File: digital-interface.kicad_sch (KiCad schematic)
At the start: 37 parts, among them U701 Si8641BD-B-IS2, U702 R05C05TE05S

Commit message: add enclosure dac sub circuit
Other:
- title: Enclosure -> Power Supply Sink
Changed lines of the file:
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@@
 	(paper "A4")
 	(title_block
-		(title "Enclosure")
+		(title "Power Supply Sink")
 		(date "2025-02-20")
-		(rev "0.1.0")
+		(rev "0.2.0")
 		(company "Open Battery Tester")
 		(comment 1 "Digital Interface")

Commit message: add enclosure power sub circuit
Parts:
- D701, D702, D704, D705: MPN UDD32C15L01 -> UDD32C24L01; VPN 603-UDD32C15L01 -> 603-UDD32C24L01
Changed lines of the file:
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@@
 		(title "Power Supply Sink")
 		(date "2025-02-20")
-		(rev "0.4.0")
+		(rev "0.5.0")
 		(company "Open Battery Tester")
 		(comment 1 "Digital Interface")
@@
 			)
 		)
-		(property "MPN" "UDD32C15L01"
+		(property "MPN" "UDD32C24L01"
 			(at 49.53 85.09 0)
 			(effects
@@
 			)
 		)
-		(property "VPN" "603-UDD32C15L01"
+		(property "VPN" "603-UDD32C24L01"
 			(at 49.53 85.09 0)
 			(effects
@@
 			)
 		)
-		(property "MPN" "UDD32C15L01"
+		(property "MPN" "UDD32C24L01"
 			(at 62.23 85.09 0)
 			(effects
@@
 			)
 		)
-		(property "VPN" "603-UDD32C15L01"
+		(property "VPN" "603-UDD32C24L01"
 			(at 62.23 85.09 0)
 			(effects
@@
 			)
 		)
-		(property "MPN" "UDD32C15L01"
+		(property "MPN" "UDD32C24L01"
 			(at 74.93 85.09 0)
 			(effects
@@
 			)
 		)
-		(property "VPN" "603-UDD32C15L01"
+		(property "VPN" "603-UDD32C24L01"
 			(at 74.93 85.09 0)
 			(effects
@@
 			)
 		)
-		(property "MPN" "UDD32C15L01"
+		(property "MPN" "UDD32C24L01"
 			(at 87.63 85.09 0)
 			(effects
@@
 			)
 		)
-		(property "VPN" "603-UDD32C15L01"
+		(property "VPN" "603-UDD32C24L01"
 			(at 87.63 85.09 0)
 			(effects

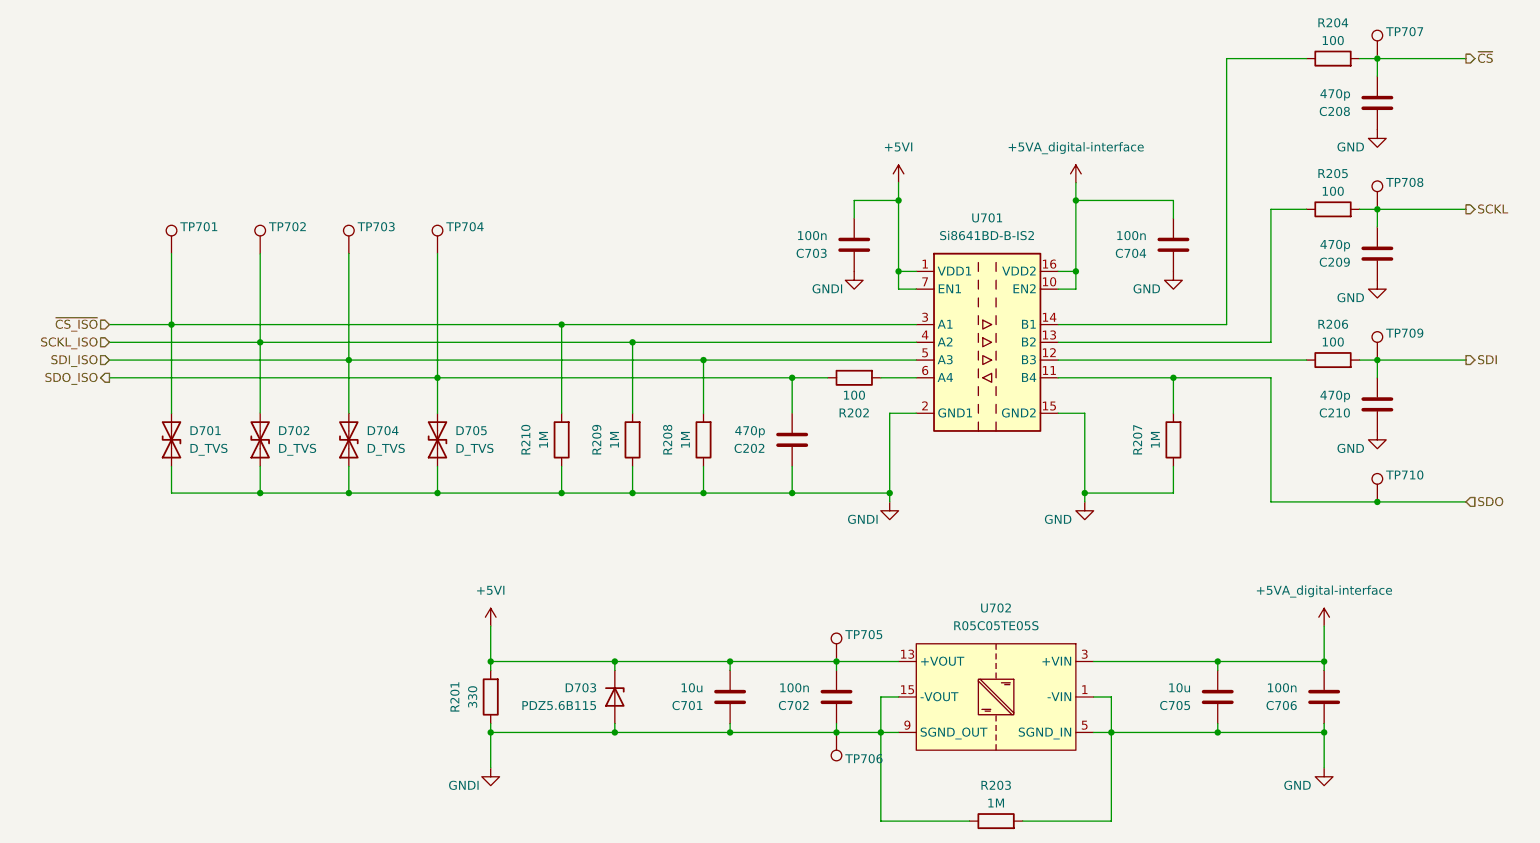
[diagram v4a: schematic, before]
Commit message: add enclosure output connectors
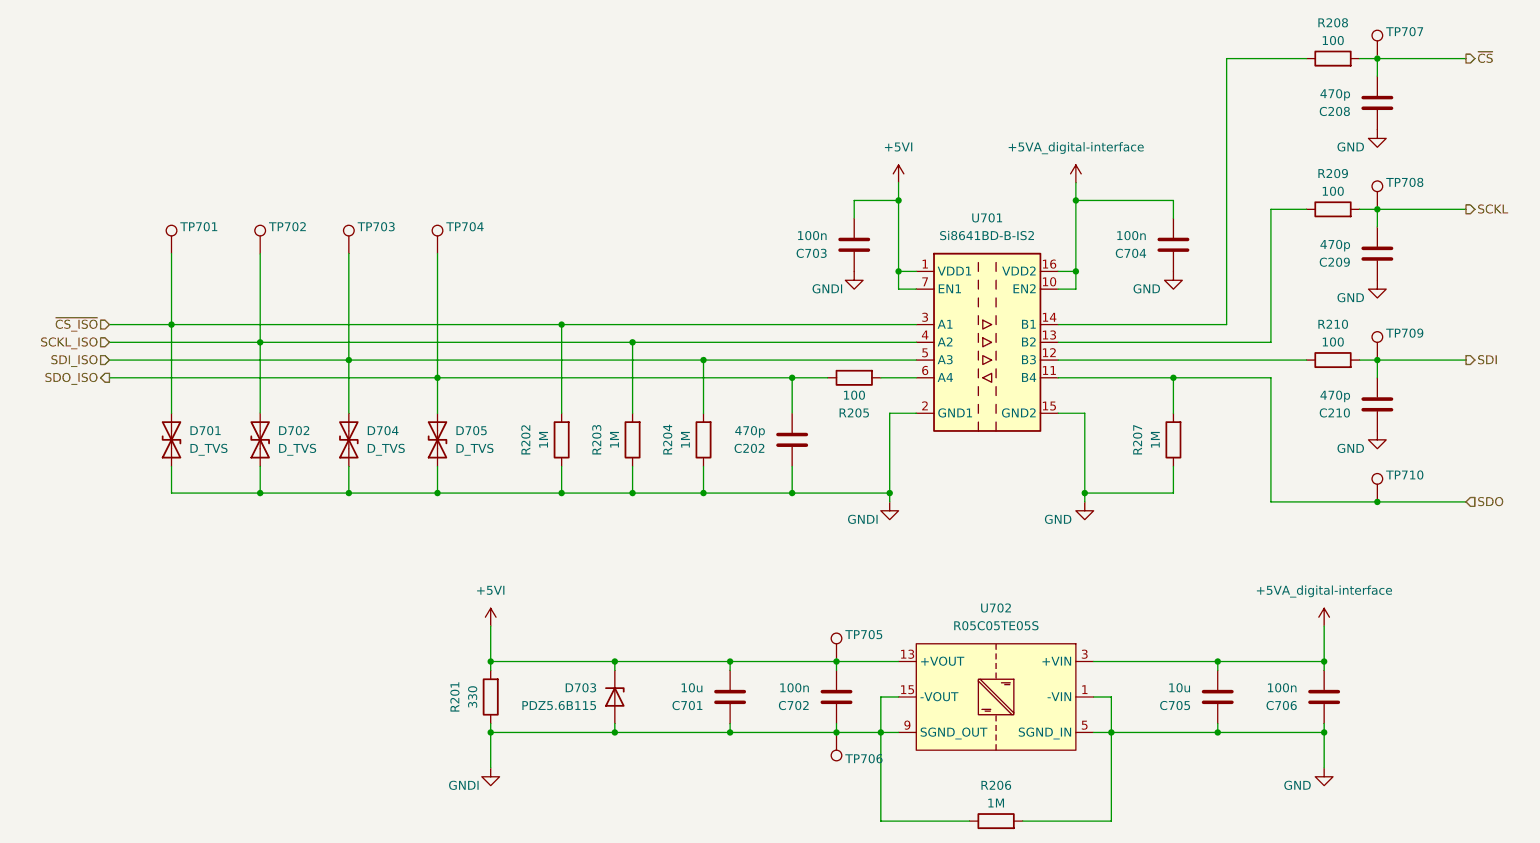
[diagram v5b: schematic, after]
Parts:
- renumbered R210 to R202, R209 to R203, R208 to R204, R202 to R205, R203 to R206, R204 to R208, R205 to R209, R206 to R210
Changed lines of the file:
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@@
 	(title_block
 		(title "Power Supply Sink")
-		(date "2025-02-20")
-		(rev "0.5.0")
+		(date "2025-02-21")
+		(rev "1.0.0")
 		(company "Open Battery Tester")
 		(comment 1 "Digital Interface")
@@
 		(on_board yes)
 		(dnp no)
-		(property "Reference" "R202"
+		(property "Reference" "R205"
 			(at 147.32 81.28 90)
 			(effects
@@
 			(project "enclosure"
 				(path "/8ec0899b-9d7b-491d-933a-49b74b34a0df/dc44c087-3b63-4db9-8fc8-89acb3b8154a"
-					(reference "R202")
+					(reference "R205")
 					(unit 1)
 				)
@@
 		(on_board yes)
 		(dnp no)
-		(property "Reference" "R203"
+		(property "Reference" "R206"
 			(at 167.64 134.62 90)
 			(effects
@@
 			(project "enclosure"
 				(path "/8ec0899b-9d7b-491d-933a-49b74b34a0df/dc44c087-3b63-4db9-8fc8-89acb3b8154a"
-					(reference "R203")
+					(reference "R206")
 					(unit 1)
 				)
@@
 		(on_board yes)
 		(dnp no)
-		(property "Reference" "R208"
+		(property "Reference" "R204"
 			(at 120.65 85.09 90)
 			(effects
@@
 			(project "enclosure"
 				(path "/8ec0899b-9d7b-491d-933a-49b74b34a0df/dc44c087-3b63-4db9-8fc8-89acb3b8154a"
-					(reference "R208")
+					(reference "R204")
 					(unit 1)
 				)
@@
 		(on_board yes)
 		(dnp no)
-		(property "Reference" "R204"
+		(property "Reference" "R208"
 			(at 215.9 25.4 90)
 			(effects
@@
 			(project "enclosure"
 				(path "/8ec0899b-9d7b-491d-933a-49b74b34a0df/dc44c087-3b63-4db9-8fc8-89acb3b8154a"
-					(reference "R204")
+					(reference "R208")
 					(unit 1)
 				)
@@
 		(on_board yes)
 		(dnp no)
-		(property "Reference" "R205"
+		(property "Reference" "R209"
 			(at 215.9 46.99 90)
 			(effects
@@
 			(project "enclosure"
 				(path "/8ec0899b-9d7b-491d-933a-49b74b34a0df/dc44c087-3b63-4db9-8fc8-89acb3b8154a"
-					(reference "R205")
+					(reference "R209")
 					(unit 1)
 				)
@@
 		(on_board yes)
 		(dnp no)
-		(property "Reference" "R206"
+		(property "Reference" "R210"
 			(at 215.9 68.58 90)
 			(effects
@@
 			(project "enclosure"
 				(path "/8ec0899b-9d7b-491d-933a-49b74b34a0df/dc44c087-3b63-4db9-8fc8-89acb3b8154a"
-					(reference "R206")
+					(reference "R210")
 					(unit 1)
 				)
@@
 		(on_board yes)
 		(dnp no)
-		(property "Reference" "R210"
+		(property "Reference" "R202"
 			(at 100.33 85.09 90)
 			(effects
@@
 			(project "enclosure"
 				(path "/8ec0899b-9d7b-491d-933a-49b74b34a0df/dc44c087-3b63-4db9-8fc8-89acb3b8154a"
-					(reference "R210")
+					(reference "R202")
 					(unit 1)
 				)
@@
 		(on_board yes)
 		(dnp no)
-		(property "Reference" "R209"
+		(property "Reference" "R203"
 			(at 110.49 85.09 90)
 			(effects
@@
 			(project "enclosure"
 				(path "/8ec0899b-9d7b-491d-933a-49b74b34a0df/dc44c087-3b63-4db9-8fc8-89acb3b8154a"
-					(reference "R209")
+					(reference "R203")
 					(unit 1)
 				)

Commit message: update datasheets and footprint references
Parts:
- C202, C208, C209, C210, C702, C703, C704, C706: footprint pss:C_0805_2012Metric_Pad1.18x1.45mm_HandSolder -> enclosure:C_0805_2012Metric_Pad1.18x1.45mm_HandSolder
- C701, C705: footprint pss:C_1210_3225Metric_Pad1.33x2.70mm_HandSolder -> enclosure:C_1210_3225Metric_Pad1.33x2.70mm_HandSolder
- D701, D702, D703, D704, D705: footprint pss:D_SOD-323_HandSoldering -> enclosure:D_SOD-323_HandSoldering
- R201, R202, R203, R204, R205, R206, R207, R208, R209, R210: footprint pss:R_1210_3225Metric_Pad1.30x2.65mm_HandSolder -> enclosure:R_1210_3225Metric_Pad1.30x2.65mm_HandSolder
- TP701, TP702, TP703, TP704, TP705, TP706, TP707, TP708, TP709, TP710: footprint pss:TP_0805_2012Metric -> enclosure:TP_0805_2012Metric
- U701, U702: footprint pss:SOIC-16W_7.5x10.3mm_P1.27mm -> enclosure:SOIC-16W_7.5x10.3mm_P1.27mm
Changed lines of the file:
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@@
 			)
 		)
-		(property "Footprint" "pss:D_SOD-323_HandSoldering"
+		(property "Footprint" "enclosure:D_SOD-323_HandSoldering"
 			(at 49.53 85.09 0)
 			(effects
@@
 			)
 		)
-		(property "Footprint" "pss:D_SOD-323_HandSoldering"
+		(property "Footprint" "enclosure:D_SOD-323_HandSoldering"
 			(at 62.23 85.09 0)
 			(effects
@@
 			)
 		)
-		(property "Footprint" "pss:C_0805_2012Metric_Pad1.18x1.45mm_HandSolder"
+		(property "Footprint" "enclosure:C_0805_2012Metric_Pad1.18x1.45mm_HandSolder"
 			(at 221.2848 33.02 0)
 			(effects
@@
 			)
 		)
-		(property "Footprint" "pss:C_0805_2012Metric_Pad1.18x1.45mm_HandSolder"
+		(property "Footprint" "enclosure:C_0805_2012Metric_Pad1.18x1.45mm_HandSolder"
 			(at 213.6648 118.11 0)
 			(effects
@@
 			)
 		)
-		(property "Footprint" "pss:TP_0805_2012Metric"
+		(property "Footprint" "enclosure:TP_0805_2012Metric"
 			(at 80.01 58.42 0)
 			(effects
@@
 			)
 		)
-		(property "Footprint" "pss:TP_0805_2012Metric"
+		(property "Footprint" "enclosure:TP_0805_2012Metric"
 			(at 227.33 52.07 0)
 			(effects
@@
 			)
 		)
-		(property "Footprint" "pss:C_0805_2012Metric_Pad1.18x1.45mm_HandSolder"
+		(property "Footprint" "enclosure:C_0805_2012Metric_Pad1.18x1.45mm_HandSolder"
 			(at 192.0748 53.34 0)
 			(effects
@@
 			)
 		)
-		(property "Footprint" "pss:TP_0805_2012Metric"
+		(property "Footprint" "enclosure:TP_0805_2012Metric"
 			(at 54.61 58.42 0)
 			(effects
@@
 			)
 		)
-		(property "Footprint" "pss:R_1210_3225Metric_Pad1.30x2.65mm_HandSolder"
+		(property "Footprint" "enclosure:R_1210_3225Metric_Pad1.30x2.65mm_HandSolder"
 			(at 147.32 74.422 90)
 			(effects
@@
 			)
 		)
-		(property "Footprint" "pss:C_1210_3225Metric_Pad1.33x2.70mm_HandSolder"
+		(property "Footprint" "enclosure:C_1210_3225Metric_Pad1.33x2.70mm_HandSolder"
 			(at 198.4248 118.11 0)
 			(effects
@@
 			)
 		)
-		(property "Footprint" "pss:R_1210_3225Metric_Pad1.30x2.65mm_HandSolder"
+		(property "Footprint" "enclosure:R_1210_3225Metric_Pad1.30x2.65mm_HandSolder"
 			(at 167.64 141.478 90)
 			(effects
@@
 			)
 		)
-		(property "Footprint" "pss:TP_0805_2012Metric"
+		(property "Footprint" "enclosure:TP_0805_2012Metric"
 			(at 227.33 93.98 0)
 			(effects
@@
 			)
 		)
-		(property "Footprint" "pss:R_1210_3225Metric_Pad1.30x2.65mm_HandSolder"
+		(property "Footprint" "enclosure:R_1210_3225Metric_Pad1.30x2.65mm_HandSolder"
 			(at 127.508 85.09 90)
 			(effects
@@
 			)
 		)
-		(property "Footprint" "pss:R_1210_3225Metric_Pad1.30x2.65mm_HandSolder"
+		(property "Footprint" "enclosure:R_1210_3225Metric_Pad1.30x2.65mm_HandSolder"
 			(at 215.9 32.258 90)
 			(effects
@@
 			)
 		)
-		(property "Footprint" "pss:D_SOD-323_HandSoldering"
+		(property "Footprint" "enclosure:D_SOD-323_HandSoldering"
 			(at 113.03 121.92 0)
 			(effects
@@
 			)
 		)
-		(property "Footprint" "pss:C_0805_2012Metric_Pad1.18x1.45mm_HandSolder"
+		(property "Footprint" "enclosure:C_0805_2012Metric_Pad1.18x1.45mm_HandSolder"
 			(at 221.2848 76.2 0)
 			(effects
@@
 			)
 		)
-		(property "Footprint" "pss:R_1210_3225Metric_Pad1.30x2.65mm_HandSolder"
+		(property "Footprint" "enclosure:R_1210_3225Metric_Pad1.30x2.65mm_HandSolder"
 			(at 97.028 121.92 90)
 			(effects
@@
 			)
 		)
-		(property "Footprint" "pss:TP_0805_2012Metric"
+		(property "Footprint" "enclosure:TP_0805_2012Metric"
 			(at 92.71 58.42 0)
 			(effects
@@
 			)
 		)
-		(property "Footprint" "pss:C_0805_2012Metric_Pad1.18x1.45mm_HandSolder"
+		(property "Footprint" "enclosure:C_0805_2012Metric_Pad1.18x1.45mm_HandSolder"
 			(at 221.2848 54.61 0)
 			(effects
@@
 			)
 		)
-		(property "Footprint" "pss:C_1210_3225Metric_Pad1.33x2.70mm_HandSolder"
+		(property "Footprint" "enclosure:C_1210_3225Metric_Pad1.33x2.70mm_HandSolder"
 			(at 128.5748 118.11 0)
 			(effects
@@
 			)
 		)
-		(property "Footprint" "pss:D_SOD-323_HandSoldering"
+		(property "Footprint" "enclosure:D_SOD-323_HandSoldering"
 			(at 74.93 85.09 0)
 			(effects
@@
 			)
 		)
-		(property "Footprint" "pss:R_1210_3225Metric_Pad1.30x2.65mm_HandSolder"
+		(property "Footprint" "enclosure:R_1210_3225Metric_Pad1.30x2.65mm_HandSolder"
 			(at 215.9 53.848 90)
 			(effects
@@
 			)
 		)
-		(property "Footprint" "pss:TP_0805_2012Metric"
+		(property "Footprint" "enclosure:TP_0805_2012Metric"
 			(at 227.33 73.66 0)
 			(effects
@@
 			)
 		)
-		(property "Footprint" "pss:SOIC-16W_7.5x10.3mm_P1.27mm"
+		(property "Footprint" "enclosure:SOIC-16W_7.5x10.3mm_P1.27mm"
 			(at 167.64 121.92 0)
 			(effects
@@
 			)
 		)
-		(property "Footprint" "pss:R_1210_3225Metric_Pad1.30x2.65mm_HandSolder"
+		(property "Footprint" "enclosure:R_1210_3225Metric_Pad1.30x2.65mm_HandSolder"
 			(at 215.9 75.438 90)
 			(effects
@@
 			)
 		)
-		(property "Footprint" "pss:TP_0805_2012Metric"
+		(property "Footprint" "enclosure:TP_0805_2012Metric"
 			(at 149.86 116.84 0)
 			(effects
@@
 			)
 		)
-		(property "Footprint" "pss:TP_0805_2012Metric"
+		(property "Footprint" "enclosure:TP_0805_2012Metric"
 			(at 67.31 58.42 0)
 			(effects
@@
 			)
 		)
-		(property "Footprint" "pss:C_0805_2012Metric_Pad1.18x1.45mm_HandSolder"
+		(property "Footprint" "enclosure:C_0805_2012Metric_Pad1.18x1.45mm_HandSolder"
 			(at 143.8148 118.11 0)
 			(effects
@@
 			)
 		)
-		(property "Footprint" "pss:TP_0805_2012Metric"
+		(property "Footprint" "enclosure:TP_0805_2012Metric"
 			(at 227.33 30.48 0)
 			(effects
@@
 			)
 		)
-		(property "Footprint" "pss:TP_0805_2012Metric"
+		(property "Footprint" "enclosure:TP_0805_2012Metric"
 			(at 149.86 127 0)
 			(effects
@@
 			)
 		)
-		(property "Footprint" "pss:R_1210_3225Metric_Pad1.30x2.65mm_HandSolder"
+		(property "Footprint" "enclosure:R_1210_3225Metric_Pad1.30x2.65mm_HandSolder"
 			(at 107.188 85.09 90)
 			(effects
@@
 			)
 		)
-		(property "Footprint" "pss:R_1210_3225Metric_Pad1.30x2.65mm_HandSolder"
+		(property "Footprint" "enclosure:R_1210_3225Metric_Pad1.30x2.65mm_HandSolder"
 			(at 117.348 85.09 90)
 			(effects
@@
 			)
 		)
-		(property "Footprint" "pss:D_SOD-323_HandSoldering"
+		(property "Footprint" "enclosure:D_SOD-323_HandSoldering"
 			(at 87.63 85.09 0)
 			(effects
@@
 			)
 		)
-		(property "Footprint" "pss:C_0805_2012Metric_Pad1.18x1.45mm_HandSolder"
+		(property "Footprint" "enclosure:C_0805_2012Metric_Pad1.18x1.45mm_HandSolder"
 			(at 137.4648 81.28 0)
 			(effects
@@
 			)
 		)
-		(property "Footprint" "pss:SOIC-16W_7.5x10.3mm_P1.27mm"
+		(property "Footprint" "enclosure:SOIC-16W_7.5x10.3mm_P1.27mm"
 			(at 166.37 85.09 0)
 			(effects
@@
 			)
 		)
-		(property "Footprint" "pss:R_1210_3225Metric_Pad1.30x2.65mm_HandSolder"
+		(property "Footprint" "enclosure:R_1210_3225Metric_Pad1.30x2.65mm_HandSolder"
 			(at 194.818 85.09 90)
 			(effects
@@
 			)
 		)
-		(property "Footprint" "pss:C_0805_2012Metric_Pad1.18x1.45mm_HandSolder"
+		(property "Footprint" "enclosure:C_0805_2012Metric_Pad1.18x1.45mm_HandSolder"
 			(at 146.3548 53.34 0)
 			(effects
